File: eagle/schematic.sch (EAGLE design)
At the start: 23 parts, among them T1 2N3904, T2 2N3904

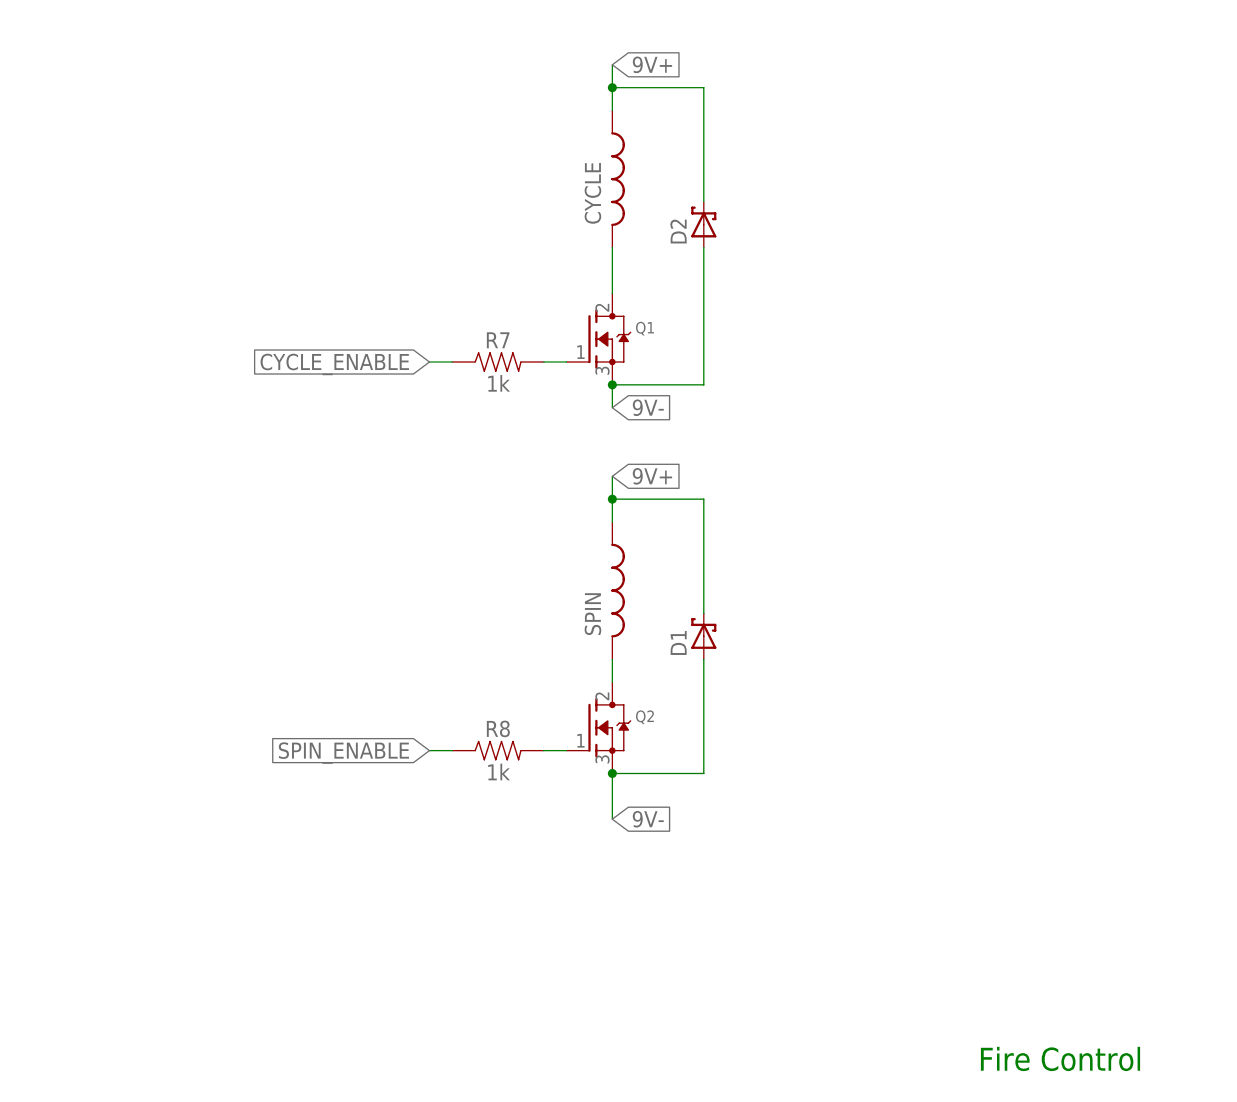
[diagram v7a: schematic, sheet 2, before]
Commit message: Correcting issue with flyback design
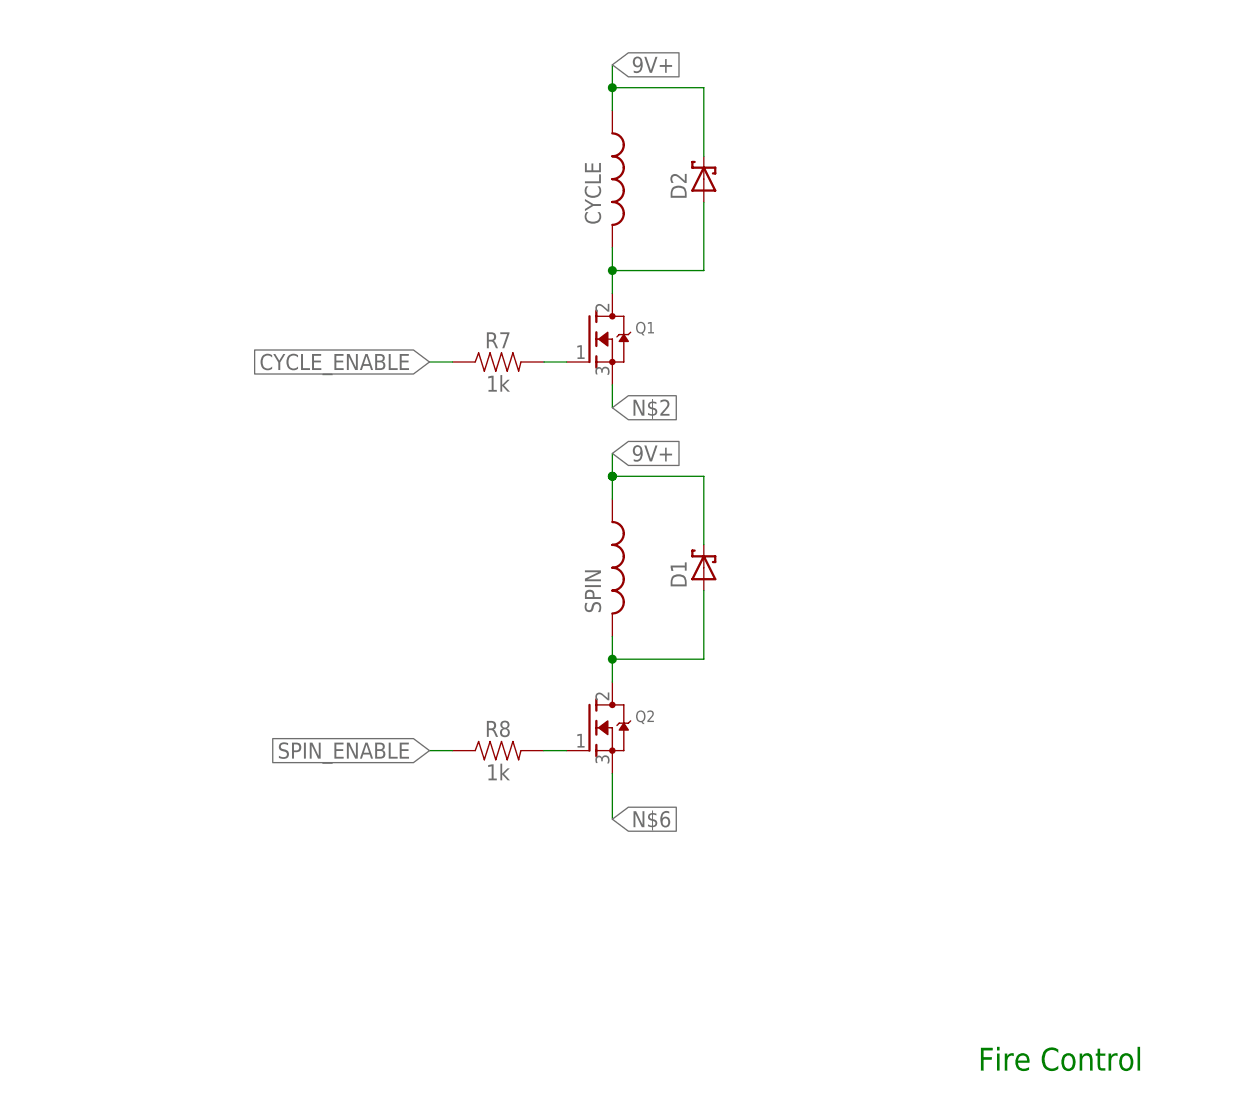
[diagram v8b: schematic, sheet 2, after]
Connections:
- removed net N$1: CYCLE.2, Q1.D
- new net N$6: Q2.S
- net 9V-: now also CYCLE.2, Q1.D, Q2.D, SPIN.2; no longer Q1.S, Q2.S
- net N$2: now also Q1.S; no longer Q2.D, SPIN.2
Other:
- moved on the sheet: D1, D2, SPIN
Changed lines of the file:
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@@
 </plain>
 <instances>
-<instance part="SPIN" gate="G$1" x="-2.54" y="48.26">
-<attribute name="NAME" x="-3.81" y="43.18" size="1.778" layer="95" rot="R90"/>
-<attribute name="VALUE" x="1.27" y="43.18" size="1.778" layer="96" rot="R90"/>
+<instance part="SPIN" gate="G$1" x="-2.54" y="50.8">
+<attribute name="NAME" x="-3.81" y="45.72" size="1.778" layer="95" rot="R90"/>
+<attribute name="VALUE" x="1.27" y="45.72" size="1.778" layer="96" rot="R90"/>
 </instance>
 <instance part="CYCLE" gate="G$1" x="-2.54" y="93.98">
@@
 <attribute name="VALUE" x="-15.24" y="28.956" size="1.778" layer="96" font="vector" align="top-center"/>
 </instance>
-<instance part="D1" gate="G$1" x="7.62" y="43.18" rot="R90">
-<attribute name="NAME" x="5.715" y="40.894" size="1.778" layer="95" rot="R90"/>
-<attribute name="VALUE" x="11.049" y="40.894" size="1.778" layer="96" rot="R90"/>
+<instance part="D1" gate="G$1" x="7.62" y="50.8" rot="R90">
+<attribute name="NAME" x="5.715" y="48.514" size="1.778" layer="95" rot="R90"/>
+<attribute name="VALUE" x="11.049" y="48.514" size="1.778" layer="96" rot="R90"/>
 </instance>
-<instance part="D2" gate="G$1" x="7.62" y="88.9" rot="R90">
-<attribute name="NAME" x="5.715" y="86.614" size="1.778" layer="95" rot="R90"/>
-<attribute name="VALUE" x="11.049" y="86.614" size="1.778" layer="96" rot="R90"/>
+<instance part="D2" gate="G$1" x="7.62" y="93.98" rot="R90">
+<attribute name="NAME" x="5.715" y="91.694" size="1.778" layer="95" rot="R90"/>
+<attribute name="VALUE" x="11.049" y="91.694" size="1.778" layer="96" rot="R90"/>
 </instance>
 </instances>
@@
 <net name="9V-" class="0">
 <segment>
-<pinref part="Q2" gate="G$1" pin="S"/>
-<wire x1="-2.54" y1="22.86" x2="-2.54" y2="27.94" width="0.1524" layer="91"/>
-<label x="-2.54" y="22.86" size="1.778" layer="95" xref="yes"/>
-<wire x1="-2.54" y1="27.94" x2="7.62" y2="27.94" width="0.1524" layer="91"/>
-<junction x="-2.54" y="27.94"/>
 <pinref part="D1" gate="G$1" pin="A"/>
-<wire x1="7.62" y1="27.94" x2="7.62" y2="40.64" width="0.1524" layer="91"/>
+<wire x1="7.62" y1="40.64" x2="7.62" y2="48.26" width="0.1524" layer="91"/>
+<pinref part="SPIN" gate="G$1" pin="2"/>
+<pinref part="Q2" gate="G$1" pin="D"/>
+<wire x1="-2.54" y1="43.18" x2="-2.54" y2="40.64" width="0.1524" layer="91"/>
+<wire x1="-2.54" y1="40.64" x2="-2.54" y2="38.1" width="0.1524" layer="91"/>
+<wire x1="7.62" y1="40.64" x2="-2.54" y2="40.64" width="0.1524" layer="91"/>
+<junction x="-2.54" y="40.64"/>
 </segment>
 <segment>
-<pinref part="Q1" gate="G$1" pin="S"/>
-<wire x1="-2.54" y1="68.58" x2="-2.54" y2="71.12" width="0.1524" layer="91"/>
-<label x="-2.54" y="68.58" size="1.778" layer="95" xref="yes"/>
-<wire x1="-2.54" y1="71.12" x2="7.62" y2="71.12" width="0.1524" layer="91"/>
-<junction x="-2.54" y="71.12"/>
 <pinref part="D2" gate="G$1" pin="A"/>
-<wire x1="7.62" y1="71.12" x2="7.62" y2="86.36" width="0.1524" layer="91"/>
+<wire x1="7.62" y1="83.82" x2="7.62" y2="91.44" width="0.1524" layer="91"/>
+<pinref part="CYCLE" gate="G$1" pin="2"/>
+<pinref part="Q1" gate="G$1" pin="D"/>
+<wire x1="-2.54" y1="86.36" x2="-2.54" y2="83.82" width="0.1524" layer="91"/>
+<wire x1="-2.54" y1="83.82" x2="-2.54" y2="81.28" width="0.1524" layer="91"/>
+<wire x1="7.62" y1="83.82" x2="-2.54" y2="83.82" width="0.1524" layer="91"/>
+<junction x="-2.54" y="83.82"/>
 </segment>
 </net>
@@
 <wire x1="-20.32" y1="30.48" x2="-22.86" y2="30.48" width="0.1524" layer="91"/>
 <label x="-22.86" y="30.48" size="1.778" layer="95" rot="R180" xref="yes"/>
-</segment>
-</net>
-<net name="N$1" class="0">
-<segment>
-<pinref part="CYCLE" gate="G$1" pin="2"/>
-<pinref part="Q1" gate="G$1" pin="D"/>
-<wire x1="-2.54" y1="86.36" x2="-2.54" y2="81.28" width="0.1524" layer="91"/>
-</segment>
-</net>
-<net name="N$2" class="0">
-<segment>
-<pinref part="SPIN" gate="G$1" pin="2"/>
-<pinref part="Q2" gate="G$1" pin="D"/>
-<wire x1="-2.54" y1="40.64" x2="-2.54" y2="38.1" width="0.1524" layer="91"/>
 </segment>
 </net>
@@
 <net name="9V+" class="0">
 <segment>
+<pinref part="D1" gate="G$1" pin="C"/>
+<wire x1="7.62" y1="53.34" x2="7.62" y2="60.96" width="0.1524" layer="91"/>
 <pinref part="SPIN" gate="G$1" pin="1"/>
+<wire x1="-2.54" y1="63.5" x2="-2.54" y2="60.96" width="0.1524" layer="91"/>
+<label x="-2.54" y="63.5" size="1.778" layer="95" xref="yes"/>
 <wire x1="-2.54" y1="60.96" x2="-2.54" y2="58.42" width="0.1524" layer="91"/>
-<label x="-2.54" y="60.96" size="1.778" layer="95" xref="yes"/>
-<pinref part="D1" gate="G$1" pin="C"/>
-<wire x1="-2.54" y1="58.42" x2="-2.54" y2="55.88" width="0.1524" layer="91"/>
-<wire x1="7.62" y1="45.72" x2="7.62" y2="58.42" width="0.1524" layer="91"/>
-<wire x1="7.62" y1="58.42" x2="-2.54" y2="58.42" width="0.1524" layer="91"/>
-<junction x="-2.54" y="58.42"/>
+<wire x1="7.62" y1="60.96" x2="-2.54" y2="60.96" width="0.1524" layer="91"/>
+<junction x="-2.54" y="60.96"/>
 </segment>
 <segment>
 <pinref part="D2" gate="G$1" pin="C"/>
-<wire x1="7.62" y1="91.44" x2="7.62" y2="104.14" width="0.1524" layer="91"/>
+<wire x1="7.62" y1="96.52" x2="7.62" y2="104.14" width="0.1524" layer="91"/>
 <junction x="-2.54" y="104.14"/>
 <wire x1="7.62" y1="104.14" x2="-2.54" y2="104.14" width="0.1524" layer="91"/>
@@
 </segment>
 </net>
+<net name="N$6" class="0">
+<segment>
+<pinref part="Q2" gate="G$1" pin="S"/>
+<wire x1="-2.54" y1="22.86" x2="-2.54" y2="27.94" width="0.1524" layer="91"/>
+<label x="-2.54" y="22.86" size="1.778" layer="95" xref="yes"/>
+</segment>
+</net>
+<net name="N$2" class="0">
+<segment>
+<pinref part="Q1" gate="G$1" pin="S"/>
+<wire x1="-2.54" y1="68.58" x2="-2.54" y2="71.12" width="0.1524" layer="91"/>
+<label x="-2.54" y="68.58" size="1.778" layer="95" xref="yes"/>
+</segment>
+</net>
+<net name="N$1" class="0">
+<segment>
+<junction x="-2.54" y="60.96"/>
+</segment>
+</net>
